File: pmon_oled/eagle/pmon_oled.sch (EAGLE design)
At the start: 36 parts, among them J1 USB, J2 USB, J4 PINHD-1X3, J5 PINHD-2X3, Q1 16Mhz, U1 LTC2943, U2 FT232RL, U3 LT1764AEQ, U4 ATMEGA328TQFP32

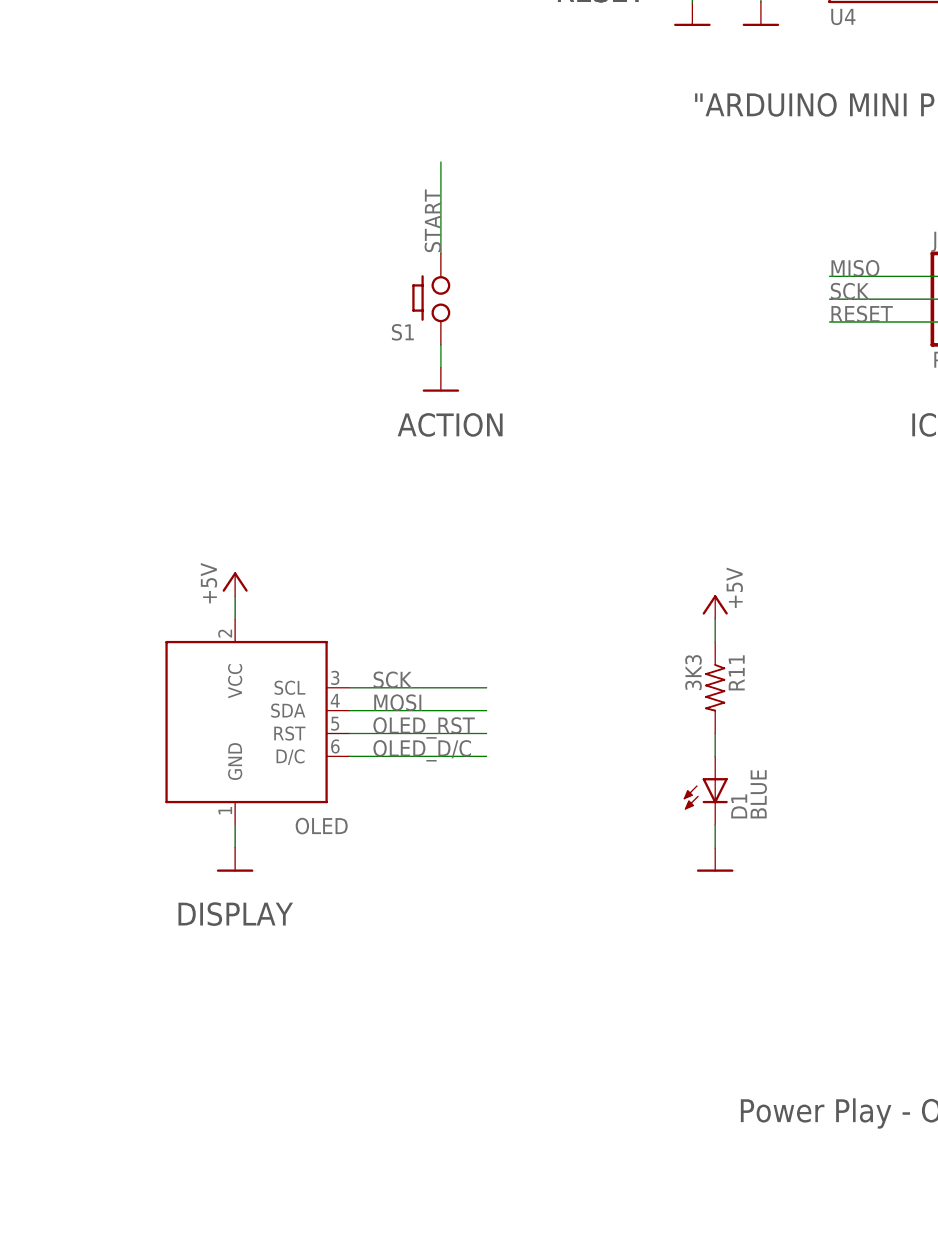
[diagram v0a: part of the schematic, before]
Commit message: Removed power led, added vias to the solder jumpers.
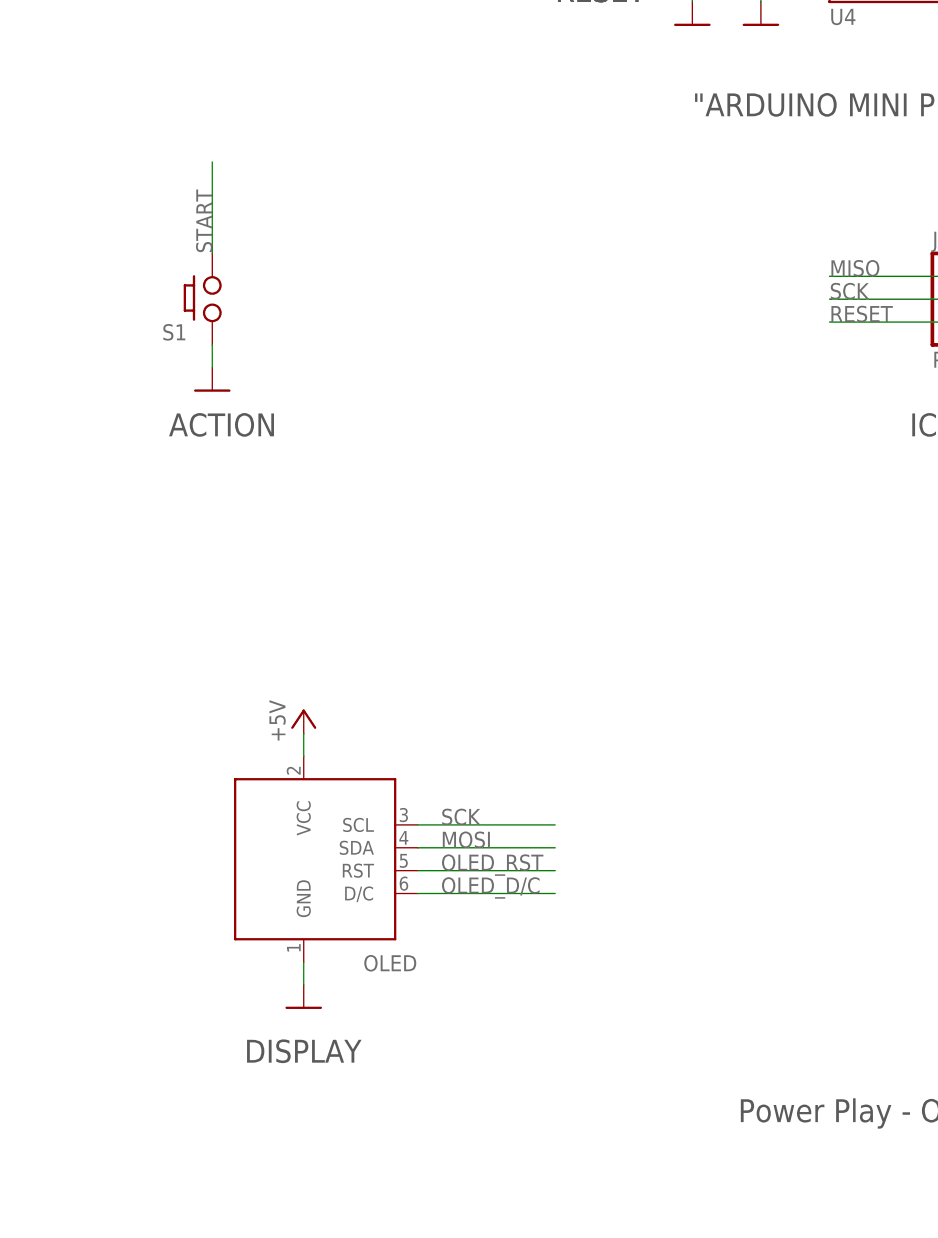
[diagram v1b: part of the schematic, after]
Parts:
- removed D1: BLUE, pmon_oled:LED1206
- removed R11: 3K3, pmon_oled:RES-R0603
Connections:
- removed net N$17: D1.A, R11.2
- net +5V: no longer R11.1
- net GND: no longer D1.C
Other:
- moved on the sheet: OLED, S1
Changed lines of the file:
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@@
 <part name="C2" library="pmon_oled" deviceset="CPOL-US" device="A/3216-18R" value="10uF"/>
 <part name="GND1" library="pmon_oled" deviceset="GND" device=""/>
-<part name="D1" library="pmon_oled" deviceset="LED" device="1206" value="BLUE"/>
-<part name="R11" library="pmon_oled" deviceset="RES-" device="R0603" value="3K3"/>
 <part name="C7" library="pmon_oled" deviceset="CAP-" device="C0603" value="0.1uF"/>
 <part name="C5" library="pmon_oled" deviceset="CAP-" device="C0603" value="0.1uF"/>
@@
 <part name="U$16" library="pmon_oled" deviceset="NC" device=""/>
 <part name="U$20" library="pmon_oled" deviceset="DOCFIELD" device=""/>
-<part name="GND18" library="pmon_oled" deviceset="GND" device=""/>
-<part name="P+3" library="pmon_oled" deviceset="+5V" device=""/>
 <part name="GND4" library="pmon_oled" deviceset="GND" device=""/>
 <part name="U3" library="pmon_oled" deviceset="LTE1764" device="" value="LT1764AEQ"/>
@@
 <text x="165.1" y="152.4" size="2.54" layer="97">RESET*</text>
 <text x="180.34" y="139.7" size="2.54" layer="97">"ARDUINO MINI PRO 328P 5V 16Mhz"</text>
-<text x="147.574" y="104.14" size="2.54" layer="97">ACTION</text>
+<text x="122.174" y="104.14" size="2.54" layer="97">ACTION</text>
 <text x="-7.112" y="213.106" size="2.54" layer="97">SOURCE</text>
-<text x="122.936" y="49.784" size="2.54" layer="97">DISPLAY</text>
+<text x="130.556" y="34.544" size="2.54" layer="97">DISPLAY</text>
 <text x="165.1" y="152.4" size="2.54" layer="97">RESET*</text>
 <text x="78.994" y="57.404" size="2.032" layer="97">Dev</text>
@@
 <instance part="C2" gate="G$1" x="12.7" y="48.26"/>
 <instance part="GND1" gate="1" x="170.18" y="208.28" rot="MR0"/>
-<instance part="D1" gate="G$1" x="182.88" y="66.04"/>
-<instance part="R11" gate="G$1" x="182.88" y="76.2" rot="R270"/>
 <instance part="C7" gate="G$1" x="68.58" y="40.64"/>
 <instance part="C5" gate="G$1" x="30.48" y="81.28" smashed="yes" rot="R270">
@@
 <instance part="U$16" gate="G$1" x="238.76" y="177.8" rot="R180"/>
 <instance part="U$20" gate="G$1" x="180.34" y="0"/>
-<instance part="GND18" gate="1" x="182.88" y="55.88" rot="MR0"/>
-<instance part="P+3" gate="1" x="182.88" y="86.36" smashed="yes">
-<attribute name="VALUE" x="185.928" y="84.836" size="1.778" layer="96" rot="R90"/>
-</instance>
 <instance part="GND4" gate="1" x="17.78" y="111.76"/>
 <instance part="U3" gate="G$1" x="55.88" y="198.12" smashed="yes">
@@
 <attribute name="VALUE" x="40.132" y="145.796" size="1.778" layer="96" rot="MR90"/>
 </instance>
-<instance part="GND22" gate="1" x="152.4" y="109.22"/>
+<instance part="GND22" gate="1" x="127" y="109.22"/>
 <instance part="J2" gate="G$1" x="-5.08" y="50.8"/>
 <instance part="Q1" gate="G$1" x="187.96" y="193.04" smashed="yes" rot="R270">
@@
 <attribute name="VALUE" x="23.876" y="212.852" size="1.778" layer="96"/>
 </instance>
-<instance part="OLED" gate="G$1" x="129.54" y="71.12" smashed="yes">
-<attribute name="NAME" x="136.144" y="59.944" size="1.778" layer="95"/>
-</instance>
-<instance part="GND33" gate="1" x="129.54" y="55.88" smashed="yes"/>
-<instance part="P+7" gate="1" x="129.54" y="88.9" smashed="yes" rot="MR0">
-<attribute name="VALUE" x="125.73" y="85.344" size="1.778" layer="96" rot="MR90"/>
+<instance part="OLED" gate="G$1" x="137.16" y="55.88" smashed="yes">
+<attribute name="NAME" x="143.764" y="44.704" size="1.778" layer="95"/>
+</instance>
+<instance part="GND33" gate="1" x="137.16" y="40.64" smashed="yes"/>
+<instance part="P+7" gate="1" x="137.16" y="73.66" smashed="yes" rot="MR0">
+<attribute name="VALUE" x="133.35" y="70.104" size="1.778" layer="96" rot="MR90"/>
 </instance>
 <instance part="U$9" gate="G$1" x="238.76" y="162.56" rot="R180"/>
@@
 </instance>
 <instance part="U$14" gate="G$1" x="238.76" y="167.64" rot="R180"/>
-<instance part="S1" gate="G$1" x="152.4" y="119.38" smashed="yes">
-<attribute name="NAME" x="146.812" y="114.808" size="1.778" layer="95"/>
+<instance part="S1" gate="G$1" x="127" y="119.38" smashed="yes">
+<attribute name="NAME" x="121.412" y="114.808" size="1.778" layer="95"/>
 </instance>
 <instance part="U$15" gate="G$1" x="238.76" y="205.74" rot="R180"/>
@@
 </segment>
 <segment>
-<pinref part="D1" gate="G$1" pin="C"/>
-<pinref part="GND18" gate="1" pin="GND"/>
-<wire x1="182.88" y1="60.96" x2="182.88" y2="58.42" width="0.1524" layer="91"/>
-</segment>
-<segment>
 <pinref part="GND15" gate="1" pin="GND"/>
 <pinref part="C5" gate="G$1" pin="2"/>
@@
 <segment>
 <pinref part="GND22" gate="1" pin="GND"/>
-<wire x1="152.4" y1="111.76" x2="152.4" y2="114.3" width="0.1524" layer="91"/>
+<wire x1="127" y1="111.76" x2="127" y2="114.3" width="0.1524" layer="91"/>
 <pinref part="S1" gate="G$1" pin="1"/>
 </segment>
@@
 <segment>
 <pinref part="OLED" gate="G$1" pin="GND"/>
-<wire x1="129.54" y1="60.96" x2="129.54" y2="58.42" width="0.1524" layer="91"/>
+<wire x1="137.16" y1="45.72" x2="137.16" y2="43.18" width="0.1524" layer="91"/>
 <pinref part="GND33" gate="1" pin="GND"/>
 </segment>
@@
 </segment>
 <segment>
-<pinref part="R11" gate="G$1" pin="1"/>
-<wire x1="182.88" y1="83.82" x2="182.88" y2="81.28" width="0.1524" layer="91"/>
-<pinref part="P+3" gate="1" pin="+5V"/>
-</segment>
-<segment>
 <pinref part="P+11" gate="1" pin="+5V"/>
 <pinref part="R2" gate="G$1" pin="2"/>
@@
 <segment>
 <pinref part="OLED" gate="G$1" pin="VCC"/>
-<wire x1="129.54" y1="83.82" x2="129.54" y2="86.36" width="0.1524" layer="91"/>
+<wire x1="137.16" y1="68.58" x2="137.16" y2="71.12" width="0.1524" layer="91"/>
 <pinref part="P+7" gate="1" pin="+5V"/>
 </segment>
@@
 </segment>
 </net>
-<net name="N$17" class="0">
-<segment>
-<pinref part="D1" gate="G$1" pin="A"/>
-<pinref part="R11" gate="G$1" pin="2"/>
-<wire x1="182.88" y1="71.12" x2="182.88" y2="68.58" width="0.1524" layer="91"/>
-</segment>
-</net>
 <net name="SCK" class="0">
 <segment>
@@
 <segment>
 <pinref part="OLED" gate="G$1" pin="SCL"/>
-<wire x1="142.24" y1="76.2" x2="157.48" y2="76.2" width="0.1524" layer="91"/>
-<label x="144.78" y="76.2" size="1.778" layer="95"/>
+<wire x1="149.86" y1="60.96" x2="165.1" y2="60.96" width="0.1524" layer="91"/>
+<label x="152.4" y="60.96" size="1.778" layer="95"/>
 </segment>
 <segment>
@@
 <segment>
 <pinref part="OLED" gate="G$1" pin="SDA"/>
-<wire x1="142.24" y1="73.66" x2="157.48" y2="73.66" width="0.1524" layer="91"/>
-<label x="144.78" y="73.66" size="1.778" layer="95"/>
+<wire x1="149.86" y1="58.42" x2="165.1" y2="58.42" width="0.1524" layer="91"/>
+<label x="152.4" y="58.42" size="1.778" layer="95"/>
 </segment>
 <segment>
@@
 </segment>
 <segment>
-<wire x1="152.4" y1="124.46" x2="152.4" y2="134.62" width="0.1524" layer="91"/>
-<label x="152.4" y="124.46" size="1.778" layer="95" rot="R90"/>
+<wire x1="127" y1="124.46" x2="127" y2="134.62" width="0.1524" layer="91"/>
+<label x="127" y="124.46" size="1.778" layer="95" rot="R90"/>
 <pinref part="S1" gate="G$1" pin="2"/>
 </segment>
@@
 <segment>
 <pinref part="OLED" gate="G$1" pin="D/C"/>
-<wire x1="142.24" y1="68.58" x2="157.48" y2="68.58" width="0.1524" layer="91"/>
-<label x="144.78" y="68.58" size="1.778" layer="95"/>
+<wire x1="149.86" y1="53.34" x2="165.1" y2="53.34" width="0.1524" layer="91"/>
+<label x="152.4" y="53.34" size="1.778" layer="95"/>
 </segment>
 </net>
@@
 <segment>
 <pinref part="OLED" gate="G$1" pin="RST"/>
-<wire x1="142.24" y1="71.12" x2="157.48" y2="71.12" width="0.1524" layer="91"/>
-<label x="144.78" y="71.12" size="1.778" layer="95"/>
-</segment>
-</net>
+<wire x1="149.86" y1="55.88" x2="165.1" y2="55.88" width="0.1524" layer="91"/>
+<label x="152.4" y="55.88" size="1.778" layer="95"/>
+</segment>
+</net>

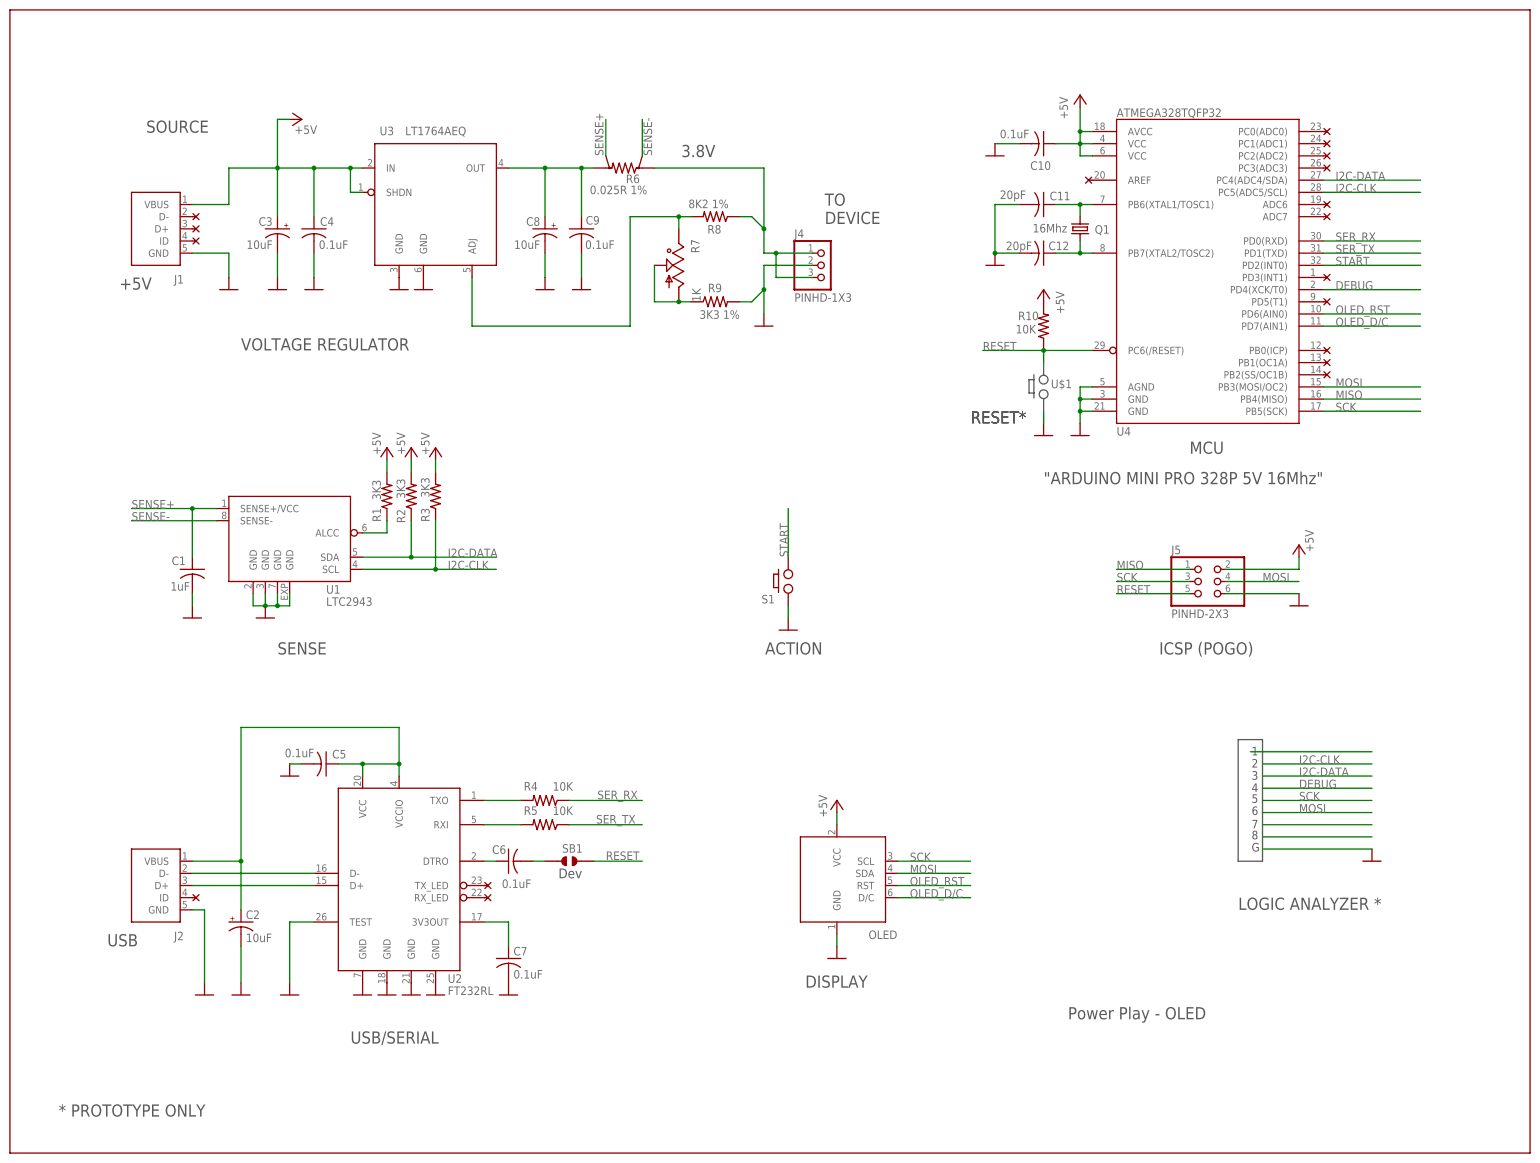
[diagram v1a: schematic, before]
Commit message: Added pmon_5v BOM. Minor tweaks of schematics and layouts.
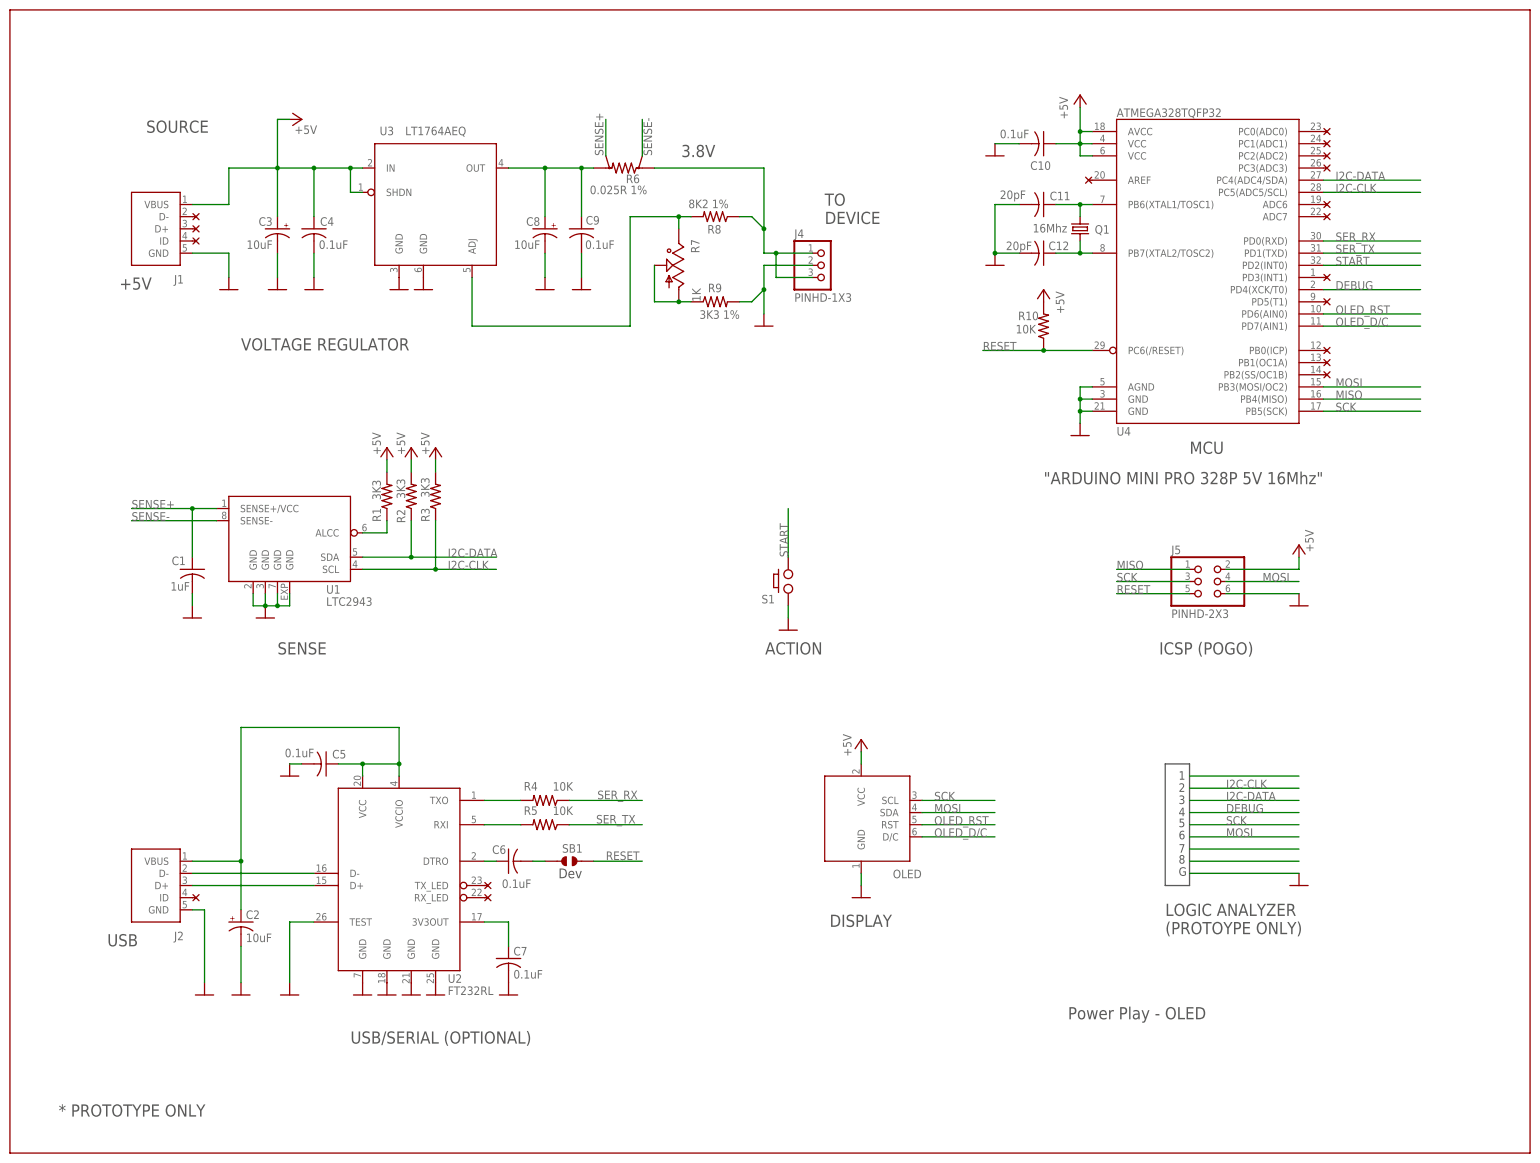
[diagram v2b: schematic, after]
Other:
- note added: "LOGIC ANALYZER (PROTOYPE ONLY)"
- note added: "USB/SERIAL (OPTIONAL)"
- note removed: "LOGIC ANALYZER *"
- note removed: "RESET*"
- note removed: "USB/SERIAL"
- moved on the sheet: OLED

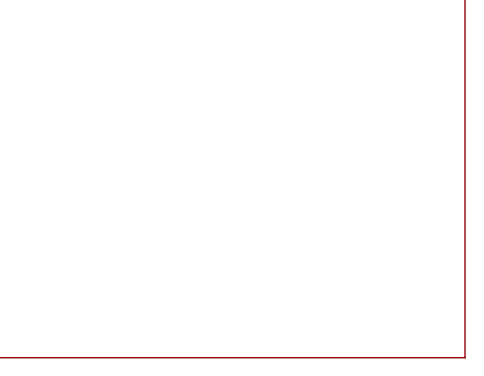
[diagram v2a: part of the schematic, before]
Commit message: Updated the LTC2943 footpting to match the datasheet (longer pads now).
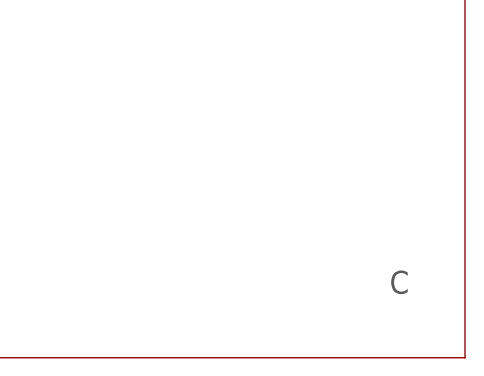
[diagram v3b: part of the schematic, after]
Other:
- note added: "C"
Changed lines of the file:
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@@
 <text x="135.636" y="47.244" size="2.54" layer="97">DISPLAY</text>
 <text x="78.994" y="57.404" size="2.032" layer="97">Dev</text>
+<text x="273.558" y="7.112" size="2.54" layer="97">C</text>
 </plain>
 <instances>
